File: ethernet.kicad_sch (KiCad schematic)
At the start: 45 parts, among them J5 Bus_RJ45_5-2337992-8, Q12 PJE138K, U10 ULS-12/5-D48N-C, U8 TPS2372-3RGWR, U9 ACPL-217-500E

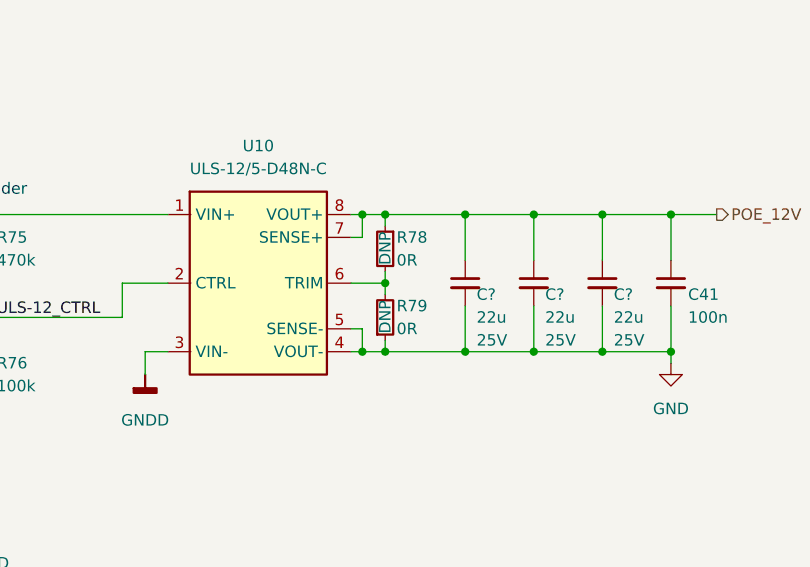
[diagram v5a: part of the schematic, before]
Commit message: [#54617] Reduce resistors diversity (switch size to 0402)
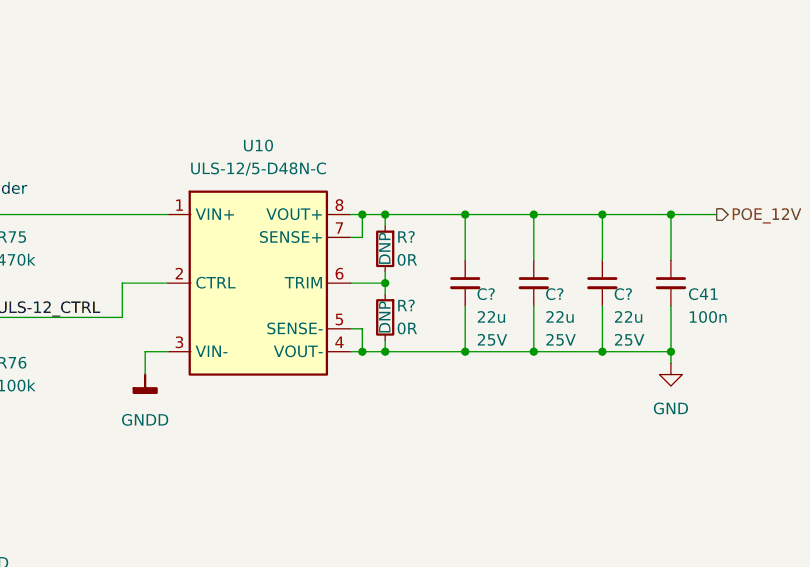
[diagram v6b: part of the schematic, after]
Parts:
- removed R78, R79: R_0R_0603, antmicro-footprints:R_0603_1608Metric, symbol antmicroResistors0603:R_0R_0603
- added R? (x2): R_0R_0402, antmicro-footprints:R_0402_1005Metric, symbol antmicroResistors0402:R_0R_0402
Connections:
- net GND: now also R?.2
- net POE_12V: now also R?.1
- net at U10.6 (TRIM): now also R?.1, R?.2
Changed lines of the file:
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@@
+    (pin "2")
+  )
+  (symbol (lib_id "antmicroResistors0402:R_0R_0402") (at 331.47 191.77 270) (unit 1)
+    (in_bom yes) (on_board yes)
+    (property "Reference" "R?" (id 0) (at 332.74 193.04 90)
+      (effects (font (size 1.27 1.27)) (justify left))
+    )
+    (property "Value" "R_0R_0402" (id 1) (at 318.77 212.09 0)
+      (effects (font (size 1.27 1.27) (thickness 0.15)) (justify left bottom) hide)
+    )
+    (property "Footprint" "antmicro-footprints:R_0402_1005Metric" (id 2) (at 316.23 212.09 0)
+      (effects (font (size 1.27 1.27) (thickness 0.15)) (justify left bottom) hide)
+    )
+    (property "Datasheet" "https://industrial.panasonic.com/cdbs/www-data/pdf/RDA0000/AOA0000C301.pdf" (id 3) (at 313.69 212.09 0)
+      (effects (font (size 1.27 1.27) (thickness 0.15)) (justify left bottom) hide)
+    )
+    (property "Manufacturer" "Panasonic" (id 4) (at 308.61 212.09 0)
+      (effects (font (size 1.27 1.27) (thickness 0.15)) (justify left bottom) hide)
+    )
+    (property "MPN" "ERJ2GE0R00X" (id 5) (at 311.15 212.09 0)
+      (effects (font (size 1.27 1.27) (thickness 0.15)) (justify left bottom) hide)
+    )
+    (property "Val" "0R" (id 6) (at 332.74 195.58 90)
+      (effects (font (size 1.27 1.27) (thickness 0.15)) (justify left))
+    )
+    (property "DNP" "DNP" (id 7) (at 331.47 194.31 0))
+    (property "License" "Apache-2.0" (id 8) (at 306.07 212.09 0)
+      (effects (font (size 1.27 1.27) (thickness 0.15)) (justify left bottom) hide)
+    )
+    (property "Author" "Antmicro" (id 9) (at 303.53 212.09 0)
+      (effects (font (size 1.27 1.27) (thickness 0.15)) (justify left bottom) hide)
+    )
+    (property "Tolerance" "~" (id 10) (at 321.31 212.09 0)
+      (effects (font (size 1.27 1.27)) (justify left bottom) hide)
+    )
+    (property "Current" "1A" (id 11) (at 330.2 191.135 0)
+      (effects (font (size 1.27 1.27) (thickness 0.15)) hide)
+    )
+    (pin "1")
     (pin "2")
   )
@@
     (pin "1")
   )
-  (symbol (lib_id "antmicroResistors0603:R_0R_0603") (at 331.47 196.85 90) (unit 1)
-    (in_bom yes) (on_board yes)
-    (property "Reference" "R79" (id 0) (at 332.74 193.04 90)
-      (effects (font (size 1.27 1.27)) (justify right))
-    )
-    (property "Value" "R_0R_0603" (id 1) (at 344.17 176.53 0)
-      (effects (font (size 1.27 1.27) (thickness 0.15)) (justify left bottom) hide)
-    )
-    (property "Footprint" "antmicro-footprints:R_0603_1608Metric" (id 2) (at 346.71 176.53 0)
-      (effects (font (size 1.27 1.27) (thickness 0.15)) (justify left bottom) hide)
-    )
-    (property "Datasheet" "https://www.bourns.com/docs/product-datasheets/cr.pdf?sfvrsn=574d41f6_14" (id 3) (at 349.25 176.53 0)
-      (effects (font (size 1.27 1.27) (thickness 0.15)) (justify left bottom) hide)
-    )
-    (property "Manufacturer" "Bourns" (id 4) (at 354.33 176.53 0)
-      (effects (font (size 1.27 1.27) (thickness 0.15)) (justify left bottom) hide)
-    )
-    (property "MPN" "CR0603-J/-000ELF" (id 5) (at 351.79 176.53 0)
-      (effects (font (size 1.27 1.27) (thickness 0.15)) (justify left bottom) hide)
-    )
-    (property "Val" "0R" (id 6) (at 332.74 195.58 90)
-      (effects (font (size 1.27 1.27) (thickness 0.15)) (justify right))
-    )
-    (property "DNP" "DNP" (id 7) (at 331.47 192.405 0)
-      (effects (font (size 1.27 1.27)) (justify right))
-    )
-    (property "License" "Apache-2.0" (id 8) (at 356.87 176.53 0)
-      (effects (font (size 1.27 1.27) (thickness 0.15)) (justify left bottom) hide)
-    )
-    (property "Author" "Antmicro" (id 9) (at 359.41 176.53 0)
-      (effects (font (size 1.27 1.27) (thickness 0.15)) (justify left bottom) hide)
-    )
-    (property "Tolerance" "~" (id 10) (at 341.63 176.53 0)
-      (effects (font (size 1.27 1.27)) (justify left bottom) hide)
-    )
-    (property "Current" "1A" (id 11) (at 334.01 198.1199 90)
-      (effects (font (size 1.27 1.27) (thickness 0.15)) (justify right) hide)
-    )
-    (pin "1")
-    (pin "2")
-  )
   (symbol (lib_id "antmicroResistors0402:R_0R_0402") (at 139.7 220.98 180) (unit 1)
     (in_bom yes) (on_board yes)
@@
     (pin "3")
     (pin "4")
+  )
+  (symbol (lib_id "antmicroResistors0402:R_0R_0402") (at 331.47 184.15 270) (unit 1)
+    (in_bom yes) (on_board yes)
+    (property "Reference" "R?" (id 0) (at 332.74 185.42 90)
+      (effects (font (size 1.27 1.27)) (justify left))
+    )
+    (property "Value" "R_0R_0402" (id 1) (at 318.77 204.47 0)
+      (effects (font (size 1.27 1.27) (thickness 0.15)) (justify left bottom) hide)
+    )
+    (property "Footprint" "antmicro-footprints:R_0402_1005Metric" (id 2) (at 316.23 204.47 0)
+      (effects (font (size 1.27 1.27) (thickness 0.15)) (justify left bottom) hide)
+    )
+    (property "Datasheet" "https://industrial.panasonic.com/cdbs/www-data/pdf/RDA0000/AOA0000C301.pdf" (id 3) (at 313.69 204.47 0)
+      (effects (font (size 1.27 1.27) (thickness 0.15)) (justify left bottom) hide)
+    )
+    (property "Manufacturer" "Panasonic" (id 4) (at 308.61 204.47 0)
+      (effects (font (size 1.27 1.27) (thickness 0.15)) (justify left bottom) hide)
+    )
+    (property "MPN" "ERJ2GE0R00X" (id 5) (at 311.15 204.47 0)
+      (effects (font (size 1.27 1.27) (thickness 0.15)) (justify left bottom) hide)
+    )
+    (property "Val" "0R" (id 6) (at 332.74 187.96 90)
+      (effects (font (size 1.27 1.27) (thickness 0.15)) (justify left))
+    )
+    (property "DNP" "DNP" (id 7) (at 331.47 186.69 0))
+    (property "License" "Apache-2.0" (id 8) (at 306.07 204.47 0)
+      (effects (font (size 1.27 1.27) (thickness 0.15)) (justify left bottom) hide)
+    )
+    (property "Author" "Antmicro" (id 9) (at 303.53 204.47 0)
+      (effects (font (size 1.27 1.27) (thickness 0.15)) (justify left bottom) hide)
+    )
+    (property "Tolerance" "~" (id 10) (at 321.31 204.47 0)
+      (effects (font (size 1.27 1.27)) (justify left bottom) hide)
+    )
+    (property "Current" "1A" (id 11) (at 330.2 183.515 0)
+      (effects (font (size 1.27 1.27) (thickness 0.15)) hide)
+    )
+    (pin "1")
+    (pin "2")
   )
   (symbol (lib_id "antmicroCapacitorsmisc:C_22u_100V_2220") (at 217.17 194.31 90) (unit 1)
@@
     )
     (pin "1")
-    (pin "2")
-  )
-  (symbol (lib_id "antmicroResistors0603:R_0R_0603") (at 331.47 184.15 270) (unit 1)
-    (in_bom yes) (on_board yes)
-    (property "Reference" "R78" (id 0) (at 332.74 185.42 90)
-      (effects (font (size 1.27 1.27)) (justify left))
-    )
-    (property "Value" "R_0R_0603" (id 1) (at 318.77 204.47 0)
-      (effects (font (size 1.27 1.27) (thickness 0.15)) (justify left bottom) hide)
-    )
-    (property "Footprint" "antmicro-footprints:R_0603_1608Metric" (id 2) (at 316.23 204.47 0)
-      (effects (font (size 1.27 1.27) (thickness 0.15)) (justify left bottom) hide)
-    )
-    (property "Datasheet" "https://www.bourns.com/docs/product-datasheets/cr.pdf?sfvrsn=574d41f6_14" (id 3) (at 313.69 204.47 0)
-      (effects (font (size 1.27 1.27) (thickness 0.15)) (justify left bottom) hide)
-    )
-    (property "Manufacturer" "Bourns" (id 4) (at 308.61 204.47 0)
-      (effects (font (size 1.27 1.27) (thickness 0.15)) (justify left bottom) hide)
-    )
-    (property "MPN" "CR0603-J/-000ELF" (id 5) (at 311.15 204.47 0)
-      (effects (font (size 1.27 1.27) (thickness 0.15)) (justify left bottom) hide)
-    )
-    (property "Val" "0R" (id 6) (at 332.74 187.96 90)
-      (effects (font (size 1.27 1.27) (thickness 0.15)) (justify left))
-    )
-    (property "DNP" "DNP" (id 7) (at 331.47 184.785 0)
-      (effects (font (size 1.27 1.27)) (justify left))
-    )
-    (property "License" "Apache-2.0" (id 8) (at 306.07 204.47 0)
-      (effects (font (size 1.27 1.27) (thickness 0.15)) (justify left bottom) hide)
-    )
-    (property "Author" "Antmicro" (id 9) (at 303.53 204.47 0)
-      (effects (font (size 1.27 1.27) (thickness 0.15)) (justify left bottom) hide)
-    )
-    (property "Tolerance" "~" (id 10) (at 321.31 204.47 0)
-      (effects (font (size 1.27 1.27)) (justify left bottom) hide)
-    )
-    (property "Current" "1A" (id 11) (at 327.66 187.96 90)
-      (effects (font (size 1.27 1.27) (thickness 0.15)) (justify left) hide)
-    )
-    (pin "1")

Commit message: [#54617] Migrate to KiCad 7
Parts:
- U10: symbol antmicroDCDCConverters:ULS-12/5-D48N-C -> antmicroDCDCConverters:ULS-12/5-D48N-C

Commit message: [#54617] Review requested changes
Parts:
- Q12: Manufacturer Panjit -> PANJIT
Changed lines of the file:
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@@
       (effects (font (size 1.27 1.27) (thickness 0.15)) (justify left bottom) hide)
     )
-    (property "Datasheet" "https://search.murata.co.jp/Ceramy/image/img/A01X/G101/ENG/GRM155R61H104KE14-01.pdf" (at 378.46 208.28 0)
+    (property "Datasheet" "https://www.murata.com/products/productdetail?partno=GRM155R61H104KE14%23" (at 378.46 208.28 0)
       (effects (font (size 1.27 1.27) (thickness 0.15)) (justify left bottom) hide)
     )
@@
       (effects (font (size 1.27 1.27) (thickness 0.15)) (justify left bottom) hide)
     )
-    (property "Datasheet" "https://www.mouser.pl/datasheet/2/1057/PJE138K-1876698.pdf" (at 290.83 220.98 0)
+    (property "Datasheet" "https://www.mouser.com/datasheet/2/1057/PJE138K-1876698.pdf" (at 290.83 220.98 0)
       (effects (font (size 1.27 1.27) (thickness 0.15)) (justify left bottom) hide)
     )
@@
       (effects (font (size 1.27 1.27) (thickness 0.15)) (justify left bottom) hide)
     )
-    (property "Manufacturer" "Panjit" (at 290.83 226.06 0)
+    (property "Manufacturer" "PANJIT" (at 290.83 226.06 0)
       (effects (font (size 1.27 1.27) (thickness 0.15)) (justify left bottom) hide)
     )
@@
       (effects (font (size 1.27 1.27) (thickness 0.15)) (justify left bottom) hide)
     )
-    (property "Datasheet" "https://search.murata.co.jp/Ceramy/image/img/A01X/G101/ENG/GRM155R71H103KA88-01.pdf" (at 166.37 109.22 0)
+    (property "Datasheet" "https://www.murata.com/products/productdetail?partno=GRM155R71H103KA88%23" (at 166.37 109.22 0)
       (effects (font (size 1.27 1.27) (thickness 0.15)) (justify left bottom) hide)
     )
@@
       (effects (font (size 1.27 1.27) (thickness 0.15)) (justify left bottom) hide)
     )
-    (property "Datasheet" "https://search.murata.co.jp/Ceramy/image/img/A01X/G101/ENG/GRM155R61H104KE14-01.pdf" (at 224.79 109.22 0)
-      (effects (font (size 1.27 1.27) (thickness 0.15)) (justify left bottom) hide)
-    )
+    (property "Datasheet" "https://www.murata.com/products/productdetail?partno=GRM155R61H104KE14%23" (at 224.79 109.22 0)
+      (effects (font (size 1.27 1.27) (thickness 0.15)) (justify left bottom) hide)
+    )
